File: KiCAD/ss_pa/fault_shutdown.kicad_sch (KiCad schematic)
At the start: 37 parts, among them J31 8P8C_Shielded, J5 Screw_Terminal_01x02, U1 LM393, U13 LM2936Z-5.0/NOPB, U2 CD74HC4066

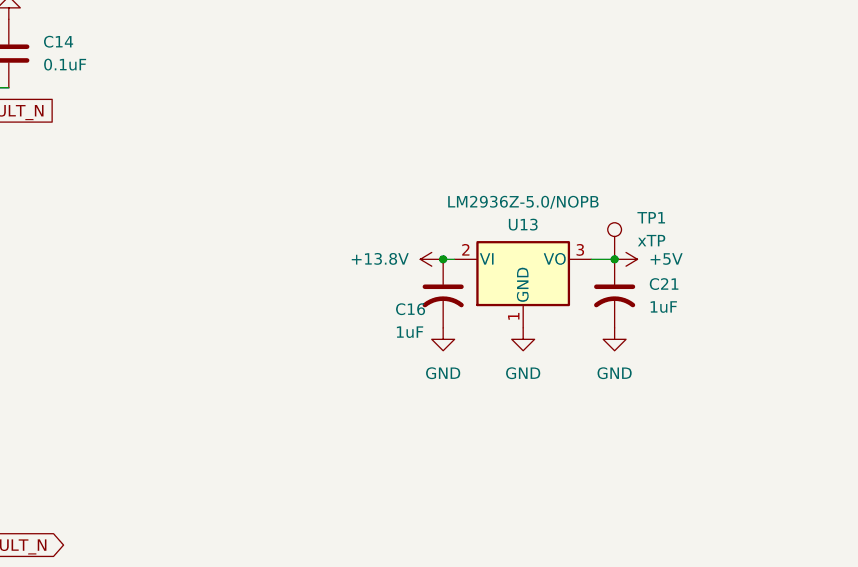
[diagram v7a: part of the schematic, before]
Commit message: revD: schematic snapshot (ss_pa U13 fix in progress) + pcb_fab_checklist §6.1
Snapshot of in-progress schematic work before the ss_pa U13 (LM2936)
pinout rework.  Netlists intentionally not regenerated here; will
follow once the ss_pa change is complete.

Documentation/pcb_fab_checklist.md: new §6.1 "Power routing guidance"
noting wide power traces throughout and star-fed +13.8V and GND through
the analog relay coils kept separate from analog signals.

Co-Authored-By: Claude Opus 4.7 <noreply@anthropic.com>
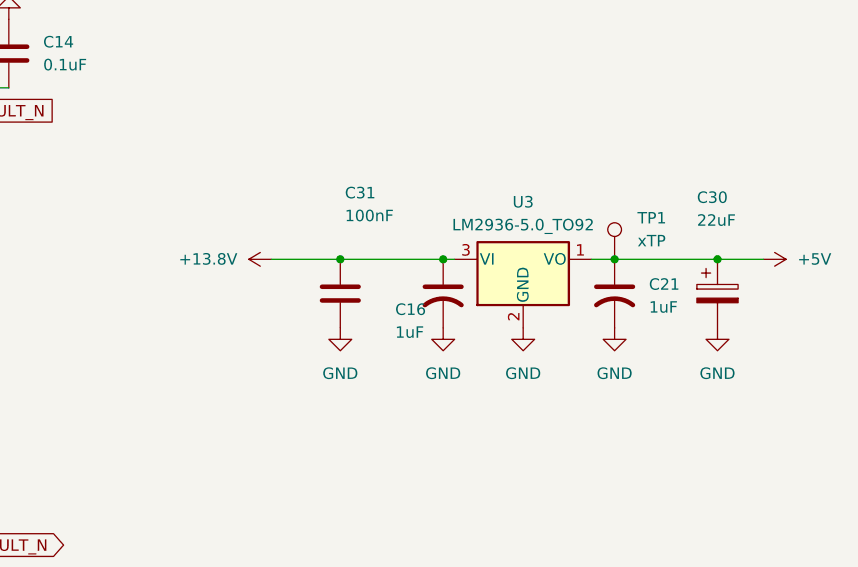
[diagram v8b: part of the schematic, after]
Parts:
- removed U13: LM2936Z-5.0/NOPB, Package_TO_SOT_THT:TO-92_Inline_Wide, symbol Regulator_Linear:MCP1700x-330xxTO
- added C30: 22uF, symbol Device:C_Polarized
- added C31: 100nF, symbol Device:C
- added U3: LM2936-5.0_TO92, Package_TO_SOT_THT:TO-92_Inline, symbol Regulator_Linear:LM2936-5.0_TO92
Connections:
- net +13.8V: now also C31.1, U3.3 (VI)
- net +5V: now also C30.1, U3.1 (VO)
- net GND: now also C30.2, C31.2, U3.2 (GND)
